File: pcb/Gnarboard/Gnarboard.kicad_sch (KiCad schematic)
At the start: 16 parts, among them J1 N2K, J2 I2C, J3 Screw_Terminal_01x12, J4 Screw_Terminal_01x12, U1 ESP32-DEVKITC, U2 MCP3208, U3 R-78B3.3-2.0

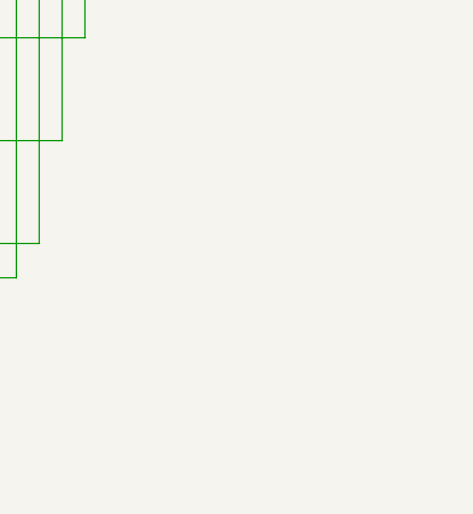
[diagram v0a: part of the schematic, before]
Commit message: added silkscreens and logos.
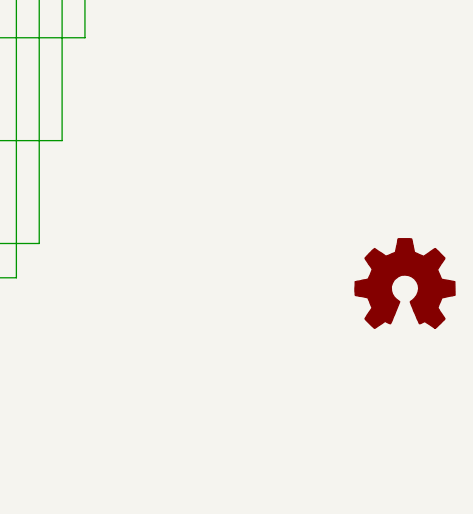
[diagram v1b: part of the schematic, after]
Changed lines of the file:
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@@
+    )
+  )
+  (symbol (lib_id "Graphic:Logo_Open_Hardware_Small") (at 275.59 158.75 0) (unit 1)
+    (in_bom no) (on_board yes) (dnp no) (fields_autoplaced)
+    (property "Reference" "#SYM1" (at 275.59 151.765 0)
+      (effects (font (size 1.27 1.27)) hide)
+    )
+    (property "Value" "Logo_Open_Hardware_Small" (at 275.59 164.465 0)
+      (effects (font (size 1.27 1.27)) hide)
+    )
+    (property "Footprint" "Symbol:OSHW-Logo2_24.3x20mm_SilkScreen" (at 275.59 158.75 0)
+      (effects (font (size 1.27 1.27)) hide)
+    )
+    (property "Datasheet" "~" (at 275.59 158.75 0)
+      (effects (font (size 1.27 1.27)) hide)
+    )
+    (property "Sim.Enable" "0" (at 275.59 158.75 0)
+      (effects (font (size 1.27 1.27)) hide)
+    )
+    (instances
+      (project "Gnarboard"
+        (path "/c83c6236-96e9-46ad-9d7a-9e2efa4a7966"
+          (reference "#SYM1") (unit 1)
+        )
+      )
     )
   )

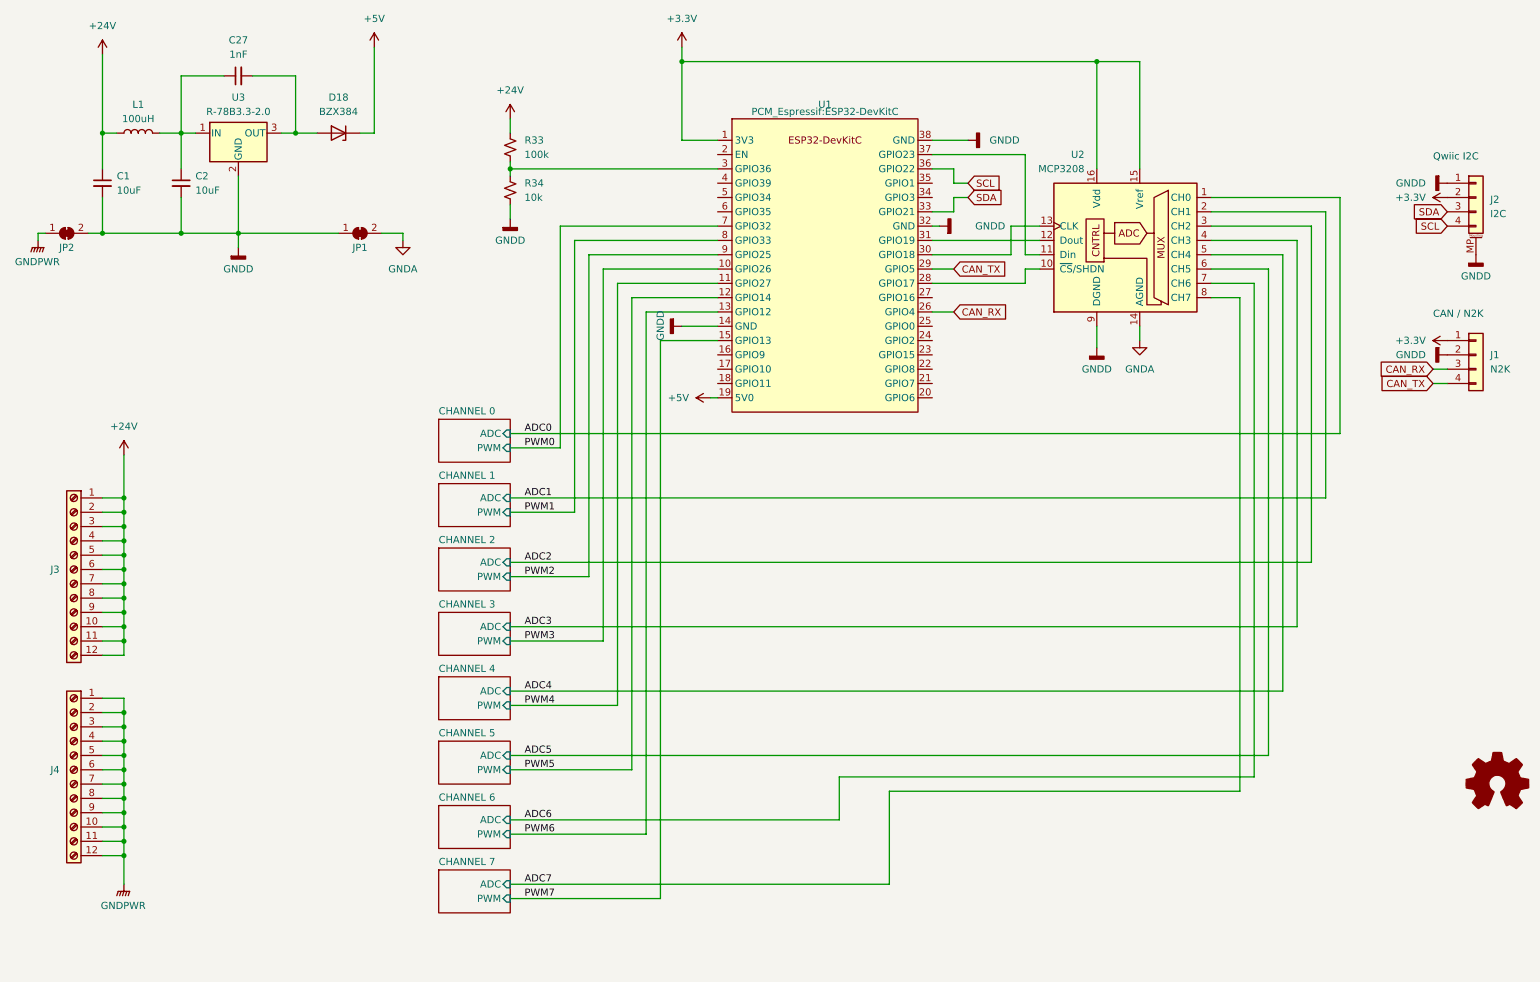
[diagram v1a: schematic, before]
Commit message: tidied up the schematic.
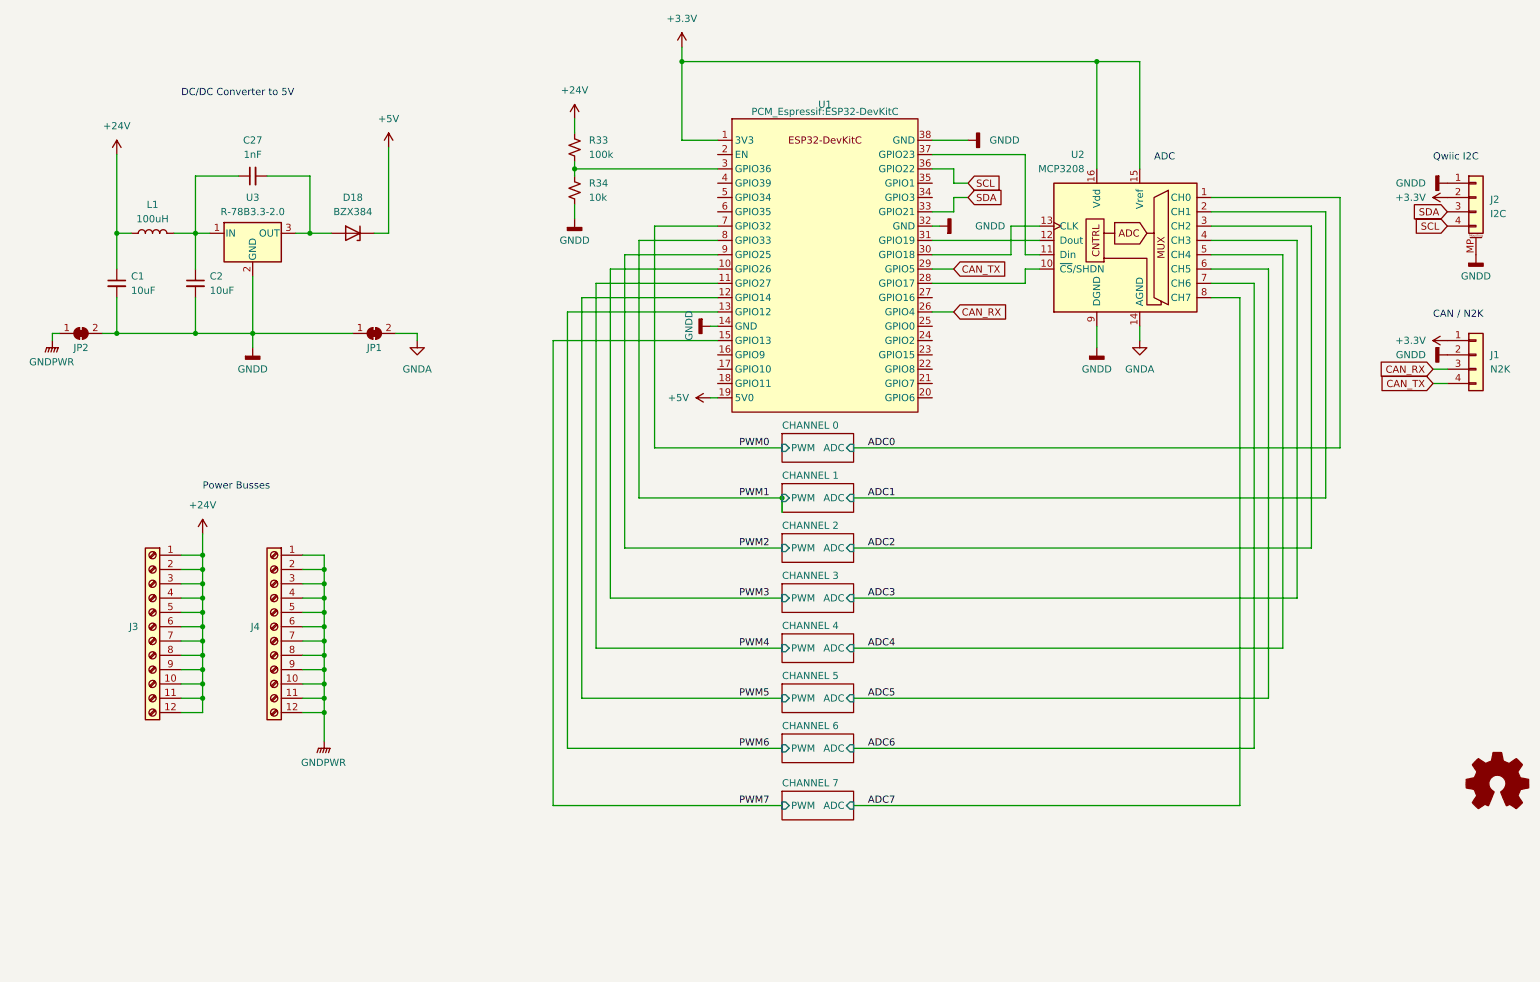
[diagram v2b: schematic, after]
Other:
- note added: "ADC"
- note added: "DC/DC Converter to 5V"
- note added: "Power Busses"
- moved on the sheet: C1, C2, C27, D18, J3, J4, JP1, JP2, L1, R33, R34, U3

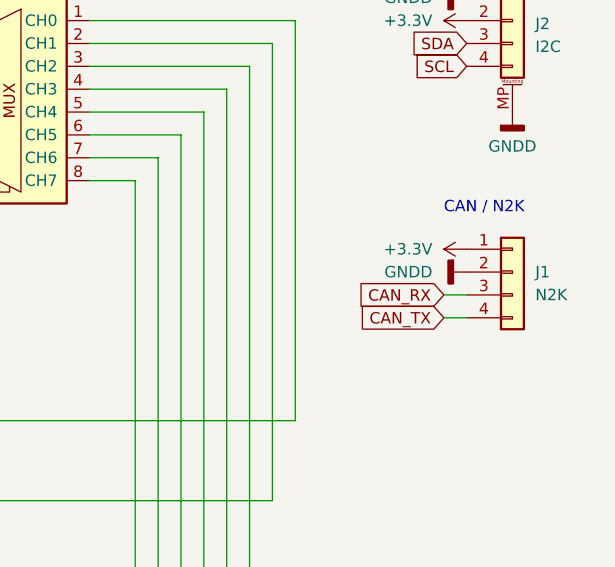
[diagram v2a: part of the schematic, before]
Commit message: updated the silkscreen and n2k connector
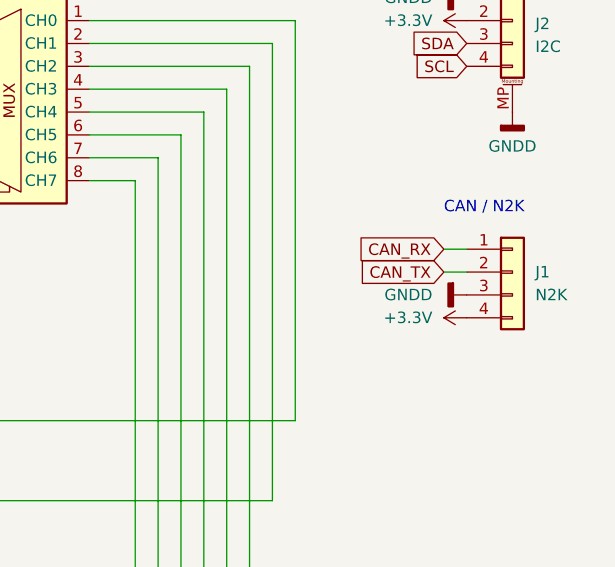
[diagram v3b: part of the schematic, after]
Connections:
- net +3.3V: now also J1.4 (Pin_4); no longer J1.1 (Pin_1)
- net CAN_RX: now also J1.1 (Pin_1); no longer J1.3 (Pin_3)
- net CAN_TX: now also J1.2 (Pin_2); no longer J1.4 (Pin_4)
- net GNDD: now also J1.3 (Pin_3); no longer J1.2 (Pin_2)
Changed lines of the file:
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@@
     (stroke (width 0) (type default))
   )
-  (wire (pts (xy 264.16 85.09) (xy 266.7 85.09))
+  (wire (pts (xy 264.16 80.01) (xy 266.7 80.01))
     (stroke (width 0) (type default))
   )
@@
     (stroke (width 0) (type default))
   )
-  (wire (pts (xy 264.16 87.63) (xy 266.7 87.63))
+  (wire (pts (xy 264.16 82.55) (xy 266.7 82.55))
     (stroke (width 0) (type default))
   )
@@
     )
   )
-  (global_label "CAN_TX" (shape input) (at 264.16 87.63 180) (fields_autoplaced)
+  (global_label "CAN_TX" (shape input) (at 264.16 82.55 180) (fields_autoplaced)
     (effects (font (size 1.27 1.27)) (justify right))
-    (property "Intersheetrefs" "${INTERSHEET_REFS}" (at 254.341 87.63 0)
+    (property "Intersheetrefs" "${INTERSHEET_REFS}" (at 254.341 82.55 0)
       (effects (font (size 1.27 1.27)) (justify right) hide)
     )
@@
     )
   )
-  (global_label "CAN_RX" (shape input) (at 264.16 85.09 180) (fields_autoplaced)
+  (global_label "CAN_RX" (shape input) (at 264.16 80.01 180) (fields_autoplaced)
     (effects (font (size 1.27 1.27)) (justify right))
-    (property "Intersheetrefs" "${INTERSHEET_REFS}" (at 254.0386 85.09 0)
+    (property "Intersheetrefs" "${INTERSHEET_REFS}" (at 254.0386 80.01 0)
       (effects (font (size 1.27 1.27)) (justify right) hide)
     )
@@
     )
   )
-  (symbol (lib_id "power:+3.3V") (at 266.7 80.01 90) (unit 1)
-    (in_bom yes) (on_board yes) (dnp no) (fields_autoplaced)
-    (property "Reference" "#PWR057" (at 270.51 80.01 0)
-      (effects (font (size 1.27 1.27)) hide)
-    )
-    (property "Value" "+3.3V" (at 262.89 80.01 90)
+  (symbol (lib_id "power:+3.3V") (at 266.7 87.63 90) (unit 1)
+    (in_bom yes) (on_board yes) (dnp no) (fields_autoplaced)
+    (property "Reference" "#PWR057" (at 270.51 87.63 0)
+      (effects (font (size 1.27 1.27)) hide)
+    )
+    (property "Value" "+3.3V" (at 262.89 87.63 90)
       (effects (font (size 1.27 1.27)) (justify left))
     )
-    (property "Footprint" "" (at 266.7 80.01 0)
-      (effects (font (size 1.27 1.27)) hide)
-    )
-    (property "Datasheet" "" (at 266.7 80.01 0)
+    (property "Footprint" "" (at 266.7 87.63 0)
+      (effects (font (size 1.27 1.27)) hide)
+    )
+    (property "Datasheet" "" (at 266.7 87.63 0)
       (effects (font (size 1.27 1.27)) hide)
     )
@@
     )
   )
-  (symbol (lib_id "power:GNDD") (at 266.7 82.55 270) (unit 1)
-    (in_bom yes) (on_board yes) (dnp no) (fields_autoplaced)
-    (property "Reference" "#PWR058" (at 260.35 82.55 0)
-      (effects (font (size 1.27 1.27)) hide)
-    )
-    (property "Value" "GNDD" (at 262.89 82.55 90)
+  (symbol (lib_id "power:GNDD") (at 266.7 85.09 270) (unit 1)
+    (in_bom yes) (on_board yes) (dnp no) (fields_autoplaced)
+    (property "Reference" "#PWR058" (at 260.35 85.09 0)
+      (effects (font (size 1.27 1.27)) hide)
+    )
+    (property "Value" "GNDD" (at 262.89 85.09 90)
       (effects (font (size 1.27 1.27)) (justify right))
     )
-    (property "Footprint" "" (at 266.7 82.55 0)
-      (effects (font (size 1.27 1.27)) hide)
-    )
-    (property "Datasheet" "" (at 266.7 82.55 0)
-      (effects (font (size 1.27 1.27)) hide)
-    )
+    (property "Footprint" "" (at 266.7 85.09 0)
+      (effects (font (size 1.27 1.27)) hide)
+    )
+    (property "Datasheet" "" (at 266.7 85.09 0)
+      (effects (font (size 1.27 1.27)) hide)
+    )

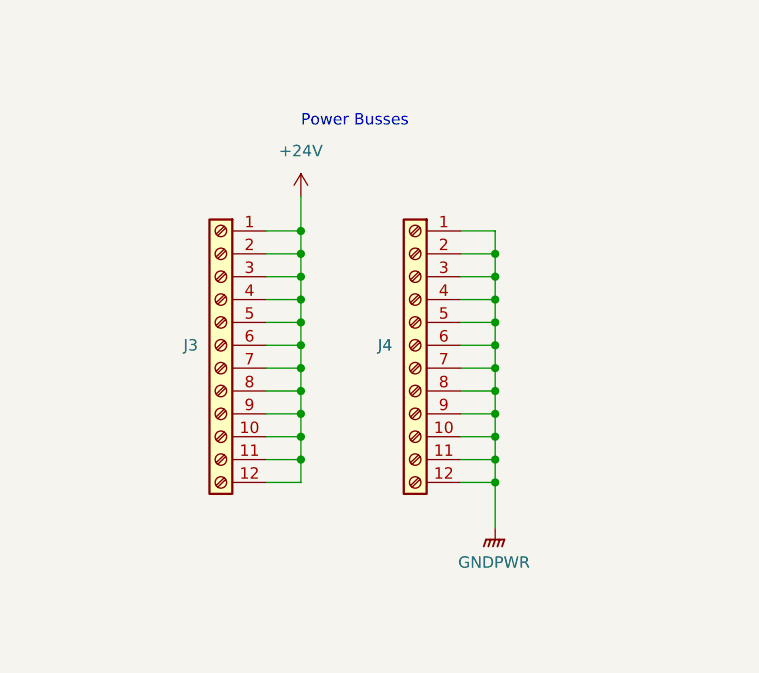
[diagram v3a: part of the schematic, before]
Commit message: changed to busbar. blueseas posts are too tall.  fml
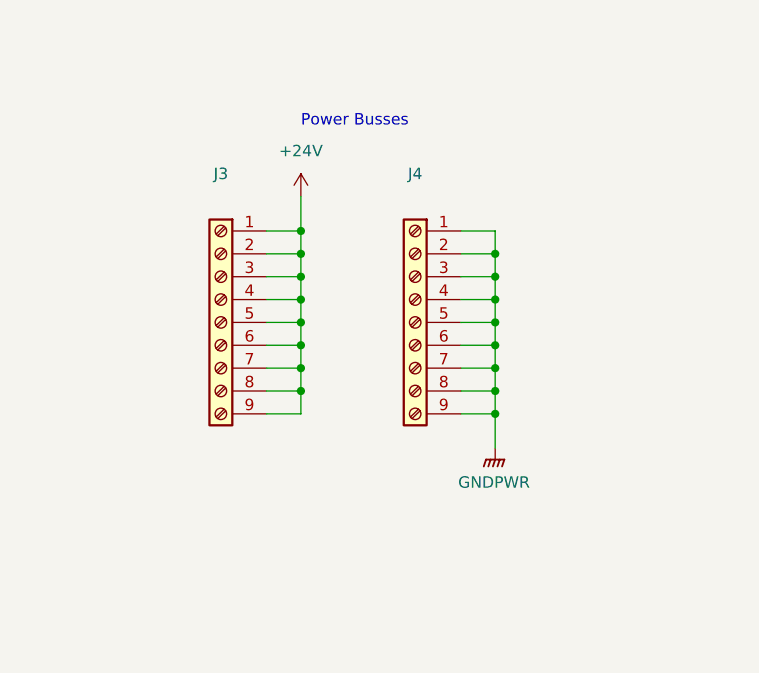
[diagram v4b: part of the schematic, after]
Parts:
- removed J3, J4: Screw_Terminal_01x12, gnarboard:BSS 2301, symbol Connector:Screw_Terminal_01x12
- added J3, J4: Screw_Terminal_01x09, gnarboard:Busbar 1x9 .375in, symbol Connector:Screw_Terminal_01x09
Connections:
- net +24V: now also J3.1 (Pin_1), J3.2 (Pin_2), J3.3 (Pin_3), J3.4 (Pin_4), J3.5 (Pin_5), J3.6 (Pin_6), J3.7 (Pin_7), J3.8 (Pin_8), J3.9 (Pin_9)
- net GNDPWR: now also J4.1 (Pin_1), J4.2 (Pin_2), J4.3 (Pin_3), J4.4 (Pin_4), J4.5 (Pin_5), J4.6 (Pin_6), J4.7 (Pin_7), J4.8 (Pin_8), J4.9 (Pin_9)
